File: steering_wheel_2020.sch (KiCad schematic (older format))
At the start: 38 parts, among them J1 VEHICLE, J10 Conn_01x15, J11 Conn_01x15, J12 ALT_PWR, J2 DEBUG, J3 Conn_01x15, J4 Conn_01x13, J5 Conn_01x15, J6 Conn_01x13, J7 Conn_01x15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

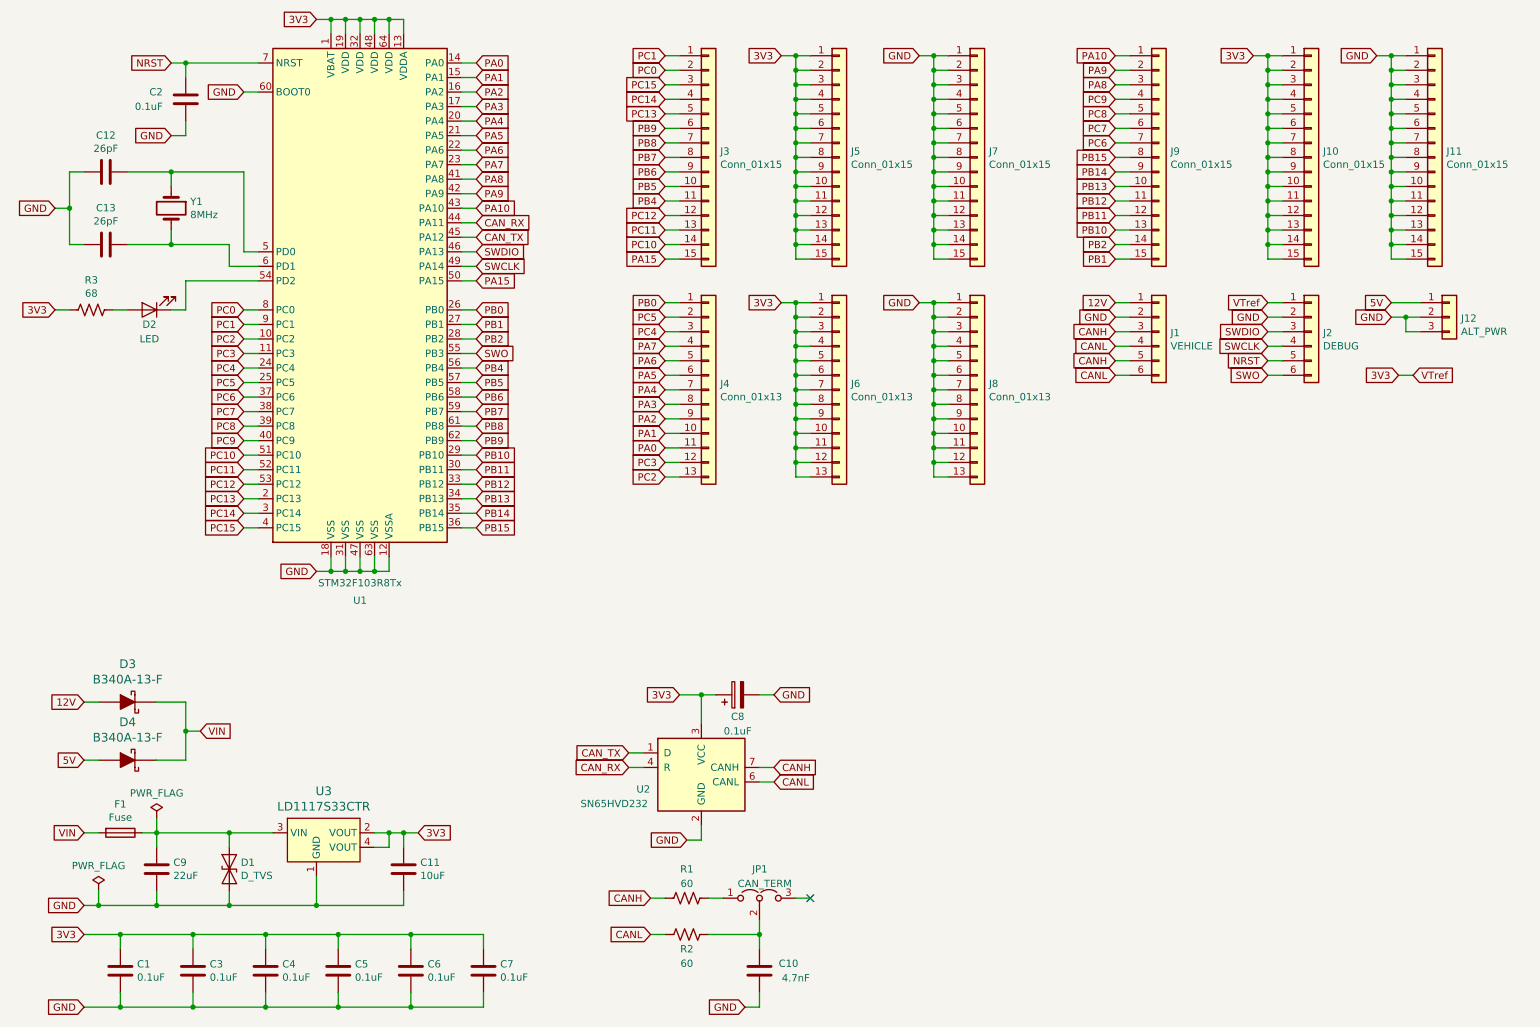
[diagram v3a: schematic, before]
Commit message: Added headers for BOOT0 and BOOT1
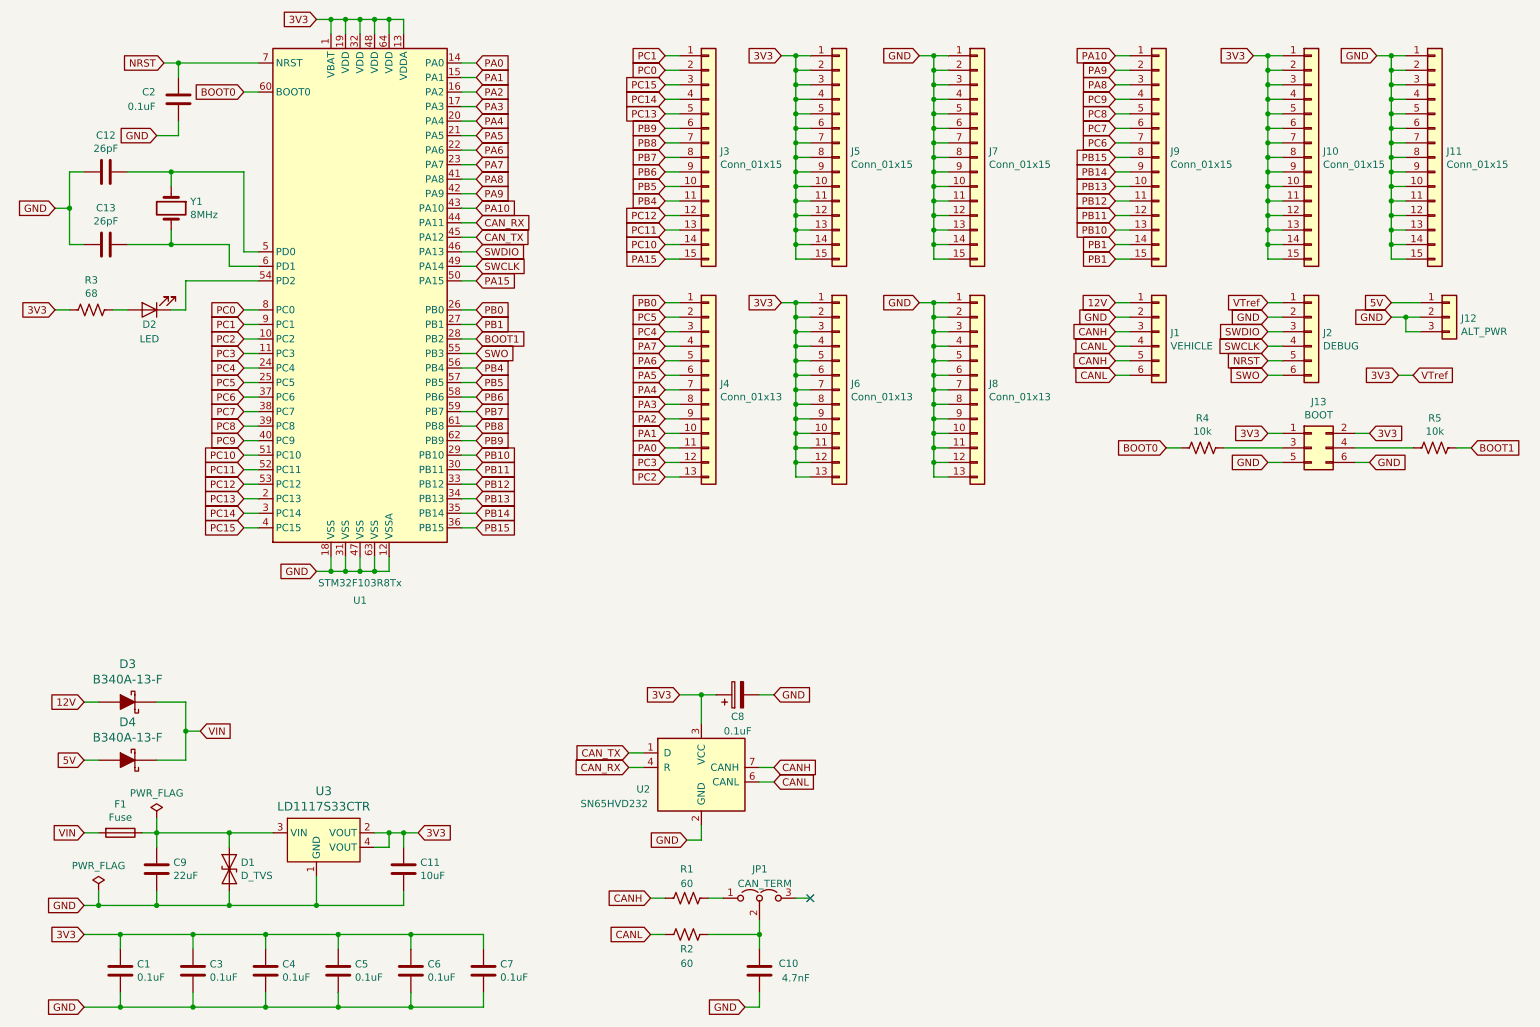
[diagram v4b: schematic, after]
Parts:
- added J13: BOOT, Connector_PinHeader_2.54mm:PinHeader_2x03_P2.54mm_Vertical, symbol Connector_Generic:Conn_02x03_Odd_Even
- added R4, R5: 10k, Resistor_SMD:R_0805_2012Metric_Pad1.15x1.40mm_HandSolder, symbol Device:R_US
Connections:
- net 3V3: now also J13.1 (Pin_1), J13.2 (Pin_2)
- net GND: now also J13.5 (Pin_5), J13.6 (Pin_6); no longer U1.60 (BOOT0)
- net PB1: now also J9.14 (Pin_14)
- net PB2 renamed BOOT1
- net BOOT1: now also R5.2; no longer J9.14 (Pin_14)
- new net: J13.3 (Pin_3), R4.1
- new net: J13.4 (Pin_4), R5.1
- new net BOOT0: R4.2, U1.60 (BOOT0)
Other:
- moved on the sheet: C2
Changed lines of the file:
@@
 EESchema Schematic File Version 4
-LIBS:steering_wheel_2020-cache
 EELAYER 30 0
 EELAYER END
@@
 PB1
 Text GLabel 8150 2250 0    50   Input ~ 0
-PB2
+PB1
 Text GLabel 5050 1950 0    50   Input ~ 0
 PB4
@@
 	3650 2900 3750 2900
 Text GLabel 3750 2900 2    50   Input ~ 0
-PB2
+BOOT1
 Wire Wire Line
 	3650 2800 3750 2800
@@
 3V3
 Wire Wire Line
-	1750 1500 1750 1400
-Wire Wire Line
-	1650 1500 1750 1500
-Text GLabel 1650 1500 0    50   Input ~ 0
+	1700 1500 1700 1400
+Wire Wire Line
+	1550 1500 1700 1500
+Text GLabel 1550 1500 0    50   Input ~ 0
 GND
 Wire Wire Line
-	1750 1000 2250 1000
-Connection ~ 1750 1000
-Wire Wire Line
-	1750 1100 1750 1000
+	1700 1000 2250 1000
+Connection ~ 1700 1000
+Wire Wire Line
+	1700 1100 1700 1000
 $Comp
 L Device:C C2
 U 1 1 5DB0163C
-P 1750 1250
-F 0 "C2" H 1500 1300 50  0000 L CNN
-F 1 "0.1uF" H 1400 1200 50  0000 L CNN
-F 2 "Capacitor_SMD:C_0805_2012Metric_Pad1.15x1.40mm_HandSolder" H 1788 1100 50  0001 C CNN
-F 3 "~" H 1750 1250 50  0001 C CNN
-	1    1750 1250
+P 1700 1250
+F 0 "C2" H 1450 1300 50  0000 L CNN
+F 1 "0.1uF" H 1350 1200 50  0000 L CNN
+F 2 "Capacitor_SMD:C_0805_2012Metric_Pad1.15x1.40mm_HandSolder" H 1738 1100 50  0001 C CNN
+F 3 "~" H 1700 1250 50  0001 C CNN
+	1    1700 1250
 	1    0    0    -1
 $EndComp
@@
 	2150 1200 2250 1200
 Text GLabel 2150 1200 0    50   Input ~ 0
-GND
+BOOT0
 Wire Wire Line
 	3650 3000 3750 3000
@@
 SWDIO
 Wire Wire Line
-	1650 1000 1750 1000
-Text GLabel 1650 1000 0    50   Input ~ 0
+	1600 1000 1700 1000
+Text GLabel 1600 1000 0    50   Input ~ 0
 NRST
 Wire Wire Line
@@
 Wire Wire Line
 	10050 2650 10250 2650
+$Comp
+L Connector_Generic:Conn_02x03_Odd_Even J13
+U 1 1 5E5FD1BC
+P 9500 3650
+F 0 "J13" H 9550 3967 50  0000 C CNN
+F 1 "BOOT" H 9550 3876 50  0000 C CNN
+F 2 "Connector_PinHeader_2.54mm:PinHeader_2x03_P2.54mm_Vertical" H 9500 3650 50  0001 C CNN
+F 3 "~" H 9500 3650 50  0001 C CNN
+	1    9500 3650
+	1    0    0    -1
+$EndComp
+Text GLabel 8500 3650 0    50   Input ~ 0
+BOOT0
+Text GLabel 9200 3550 0    50   Input ~ 0
+3V3
+Wire Wire Line
+	9200 3550 9300 3550
+Text GLabel 9200 3750 0    50   Input ~ 0
+GND
+Wire Wire Line
+	9200 3750 9300 3750
+Text GLabel 9900 3750 2    50   Input ~ 0
+GND
+Wire Wire Line
+	9800 3750 9900 3750
+Text GLabel 10600 3650 2    50   Input ~ 0
+BOOT1
+Text GLabel 9900 3550 2    50   Input ~ 0
+3V3
+Wire Wire Line
+	9800 3550 9900 3550
+$Comp
+L Device:R_US R4
+U 1 1 5E80EE60
+P 8750 3650
+F 0 "R4" V 8545 3650 50  0000 C CNN
+F 1 "10k" V 8636 3650 50  0000 C CNN
+F 2 "Resistor_SMD:R_0805_2012Metric_Pad1.15x1.40mm_HandSolder" V 8790 3640 50  0001 C CNN
+F 3 "~" H 8750 3650 50  0001 C CNN
+	1    8750 3650
+	0    1    1    0
+$EndComp
+Wire Wire Line
+	8900 3650 9300 3650
+Wire Wire Line
+	8500 3650 8600 3650
+$Comp
+L Device:R_US R5
+U 1 1 5E8DE641
+P 10350 3650
+F 0 "R5" V 10555 3650 50  0000 C CNN
+F 1 "10k" V 10464 3650 50  0000 C CNN
+F 2 "Resistor_SMD:R_0805_2012Metric_Pad1.15x1.40mm_HandSolder" V 10390 3640 50  0001 C CNN
+F 3 "~" H 10350 3650 50  0001 C CNN
+	1    10350 3650
+	0    -1   -1   0
+$EndComp
+Wire Wire Line
+	10500 3650 10600 3650
+Wire Wire Line
+	9800 3650 10200 3650
 $EndSCHEMATC
